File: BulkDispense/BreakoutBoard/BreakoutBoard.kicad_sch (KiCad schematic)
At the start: 35 parts, among them J1 BS1, J10 OS3, J11 OS4, J12 FS1, J13 FS3, J14 PCV, J15 FS2, J16 FS4, J17 WL1, J18 WL2, J19 Analog Inputs, J2 BS2, J20 R0~R3, J21 R4~R7, J22 R8~R9, J23 Digital IN + R0~R4, J24 WB1, J25 WB2, J26 Digital Outputs, J27 R4~R9, J28 WV1, J29 WV2, J3 OS1, J30 Flow Sensors, J4 OS2, J5 PS, J6 MV1&2, J7 MV3&4, J8 BS3, J9 BS4

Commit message: Design Overhaul
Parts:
- removed J1: BS1, PartsLibrary:3720362A3003PL, symbol Connector:Conn_01x03_Socket
- removed J10: OS3, PartsLibrary:3720362A3003PL, symbol Connector:Conn_01x03_Socket
- removed J11: OS4, PartsLibrary:3720362A3003PL, symbol Connector:Conn_01x03_Socket
- removed J19: Analog Inputs, PartsLibrary:CONN_37212-62M3-003PL_3MM, symbol Connector:Conn_01x12_Socket
- removed J2: BS2, PartsLibrary:3720362A3003PL, symbol Connector:Conn_01x03_Socket
- removed J21: R4~R7, PartsLibrary:CONN_37204-62A3-004PL_3MM, symbol Connector:Conn_01x04_Socket
- removed J22: R8~R9, PartsLibrary:CONN_37204-62A3-004PL_3MM, symbol Connector:Conn_01x04_Socket
- removed J26: Digital Outputs, PartsLibrary:CONN_37212-62M3-003PL_3MM, symbol Connector:Conn_01x12_Socket
- removed J28: WV1, PartsLibrary:3720362A3003PL, symbol Connector:Conn_01x03_Socket
- removed J29: WV2, PartsLibrary:3720362A3003PL, symbol Connector:Conn_01x03_Socket
- removed J3: OS1, PartsLibrary:3720362A3003PL, symbol Connector:Conn_01x03_Socket
- removed J4: OS2, PartsLibrary:3720362A3003PL, symbol Connector:Conn_01x03_Socket
- removed J8: BS3, PartsLibrary:3720362A3003PL, symbol Connector:Conn_01x03_Socket
- removed J9: BS4, PartsLibrary:3720362A3003PL, symbol Connector:Conn_01x03_Socket
- removed MAXI1: ~, symbol SymbolLibrary:Controllino_MAXI
- added H5: MountingHole, MountingHole:MountingHole_3.2mm_M3, symbol Mechanical:MountingHole
- added J13: DigitalOUT 0~3, PartsLibrary:CONN_37204-62A3-004PL_3MM, symbol Connector:Conn_01x04_Socket
- added J14: DigitalOUT 4~7, PartsLibrary:CONN_37204-62A3-004PL_3MM, symbol Connector:Conn_01x04_Socket
- added J18: WB-MV1&2, PartsLibrary:CONN_37204-62A3-004PL_3MM, symbol Connector:Conn_01x04_Socket
- added J19: WB-MV3&4, PartsLibrary:CONN_37204-62A3-004PL_3MM, symbol Connector:Conn_01x04_Socket
- added J20: FS1, PartsLibrary:CONN_37204-62A3-004PL_3MM, symbol Connector:Conn_01x04_Socket
- added J22: WB-MV5&6, PartsLibrary:3720362A3003PL, symbol Connector:Conn_01x03_Socket
- H1, H2, H3, H4: footprint MountingHole:MountingHole_2.2mm_M2 -> MountingHole:MountingHole_3.2mm_M3
- J10: renamed from J23; value Digital IN + R0~R4 -> R0~R5
- J17: renamed from J27; value R4~R9 -> AnalogIOs
- J21: renamed from J30; value Flow Sensors -> FS2~FS4
- J4: renamed from J20; value R0~R3 -> RV1~4
- renumbered J5 to J1, J17 to J11, J18 to J12, J24 to J15, J25 to J16, J6 to J2, J7 to J3, J14 to J5, J12 to J6, J13 to J7, J15 to J8, J16 to J9
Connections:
- net DI0 is gone; now on net +24V: J10.1 (Pin_1)
- net DI1 is gone; now on net +24V: J10.2 (Pin_2)
- net DI2 is gone; now on net +24V: J10.3 (Pin_3)
- net DI3 is gone; now on net +24V: J10.4 (Pin_4)
- net R7_OUT is gone; now on net +24V: J17.10 (Pin_10)
- net R9_OUT is gone; now on net GND: J17.12 (Pin_12)
- net +24V: no longer J10.7 (Pin_7), J10.8 (Pin_8), J17.1 (Pin_1), J17.2 (Pin_2), J17.3 (Pin_3), J17.4 (Pin_4), J17.5 (Pin_5), J17.6 (Pin_6)
- net AI12: now also J17.5 (Pin_5)
- net AI13: now also J17.6 (Pin_6)
- net AI4: now also J17.1 (Pin_1)
- net AI5: now also J17.2 (Pin_2)
- net AI6: now also J17.3 (Pin_3)
- net AI7: now also J17.4 (Pin_4)
- net AO0: now also J17.8 (Pin_8); no longer J21.11 (Pin_11)
- net DO0: now also J13.1 (Pin_1)
- net DO1: now also J13.2 (Pin_2)
- net DO2: now also J13.3 (Pin_3)
- net DO3: now also J13.4 (Pin_4)
- net FS1-1: now also J20.1 (Pin_1)
- net FS1-2: now also J20.2 (Pin_2)
- net FS1-3: now also J20.3 (Pin_3)
- net FS1-4: now also J20.4 (Pin_4)
- net FS2-1: now also J21.1 (Pin_1)
- net FS2-2: now also J21.2 (Pin_2)
- net FS2-3: now also J21.3 (Pin_3); no longer J21.1 (Pin_1)
- net FS2-4: now also J21.4 (Pin_4); no longer J21.2 (Pin_2)
- net FS3-1: now also J21.5 (Pin_5); no longer J21.3 (Pin_3)
- net FS3-2: now also J21.6 (Pin_6); no longer J21.4 (Pin_4)
- net FS3-3: now also J21.7 (Pin_7); no longer J21.5 (Pin_5)
- net FS3-4: now also J21.8 (Pin_8); no longer J21.6 (Pin_6)
- net FS4-1: now also J21.9 (Pin_9); no longer J21.7 (Pin_7)
- net FS4-2: now also J21.10 (Pin_10); no longer J21.8 (Pin_8)
- net FS4-3: now also J21.11 (Pin_11); no longer J21.9 (Pin_9)
- net FS4-4: now also J21.12 (Pin_12); no longer J21.10 (Pin_10)
- net GND: now also J18.2 (Pin_2), J18.4 (Pin_4), J19.2 (Pin_2), J19.4 (Pin_4)
- net R0_OUT: now also J10.7 (Pin_7); no longer J10.9 (Pin_9)
- net R1_OUT: now also J10.8 (Pin_8); no longer J10.10 (Pin_10)
- net R2_OUT: now also J10.9 (Pin_9); no longer J10.11 (Pin_11)
- net R3_OUT: now also J10.10 (Pin_10); no longer J10.12 (Pin_12)
- net R4_OUT: now also J10.11 (Pin_11), J22.1 (Pin_1); no longer J17.7 (Pin_7)
- net R5_OUT: now also J10.12 (Pin_12), J22.3 (Pin_3); no longer J17.8 (Pin_8)
- net R6_OUT: no longer names the net of J17.9 (Pin_9)
- net R8_OUT: no longer names the net of J17.11 (Pin_11)
- new net DO4: J14.1 (Pin_1), J18.1 (Pin_1)
- new net DO5: J14.2 (Pin_2), J18.3 (Pin_3)
- new net DO6: J14.3 (Pin_3), J19.1 (Pin_1)
- new net DO7: J14.4 (Pin_4), J19.3 (Pin_3)
- no-connect marks 1 -> 4
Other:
- note added: "WB-MV1"
- note added: "WB-MV2"
- note added: "WB-MV3"
- note added: "WB-MV4"
- note removed: "Relays"
- moved on the sheet: J1, J10, J15, J16, J17, J2, J21, J3, J4, J5, J6, J7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

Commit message: Add latest design
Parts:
- added J24: LDS, PartsLibrary:CONN_37204-62A3-004PL_3MM, symbol Connector:Conn_01x04_Socket
- J11, J12, J15, J16, J22: footprint PartsLibrary:3720362A3003PL -> PartsLibrary:CONN_37203-62A3-003PL_3MM
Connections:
- net +24V: now also J17.11 (Pin_11); no longer J17.10 (Pin_10)
- net AO0: now also J17.7 (Pin_7); no longer J17.8 (Pin_8)
- net LDS-GND: now reaches J17.9 (Pin_9)
- net LDS-GND: now also J24.2 (Pin_2)
- new net LDS: J17.10 (Pin_10), J24.3 (Pin_3)
- new net LDS-5V: J17.8 (Pin_8), J24.1 (Pin_1)
- no-connect marks 4 -> 2
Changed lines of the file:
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@@
 	(rectangle
 		(start 21.59 57.15)
-		(end 106.68 157.48)
+		(end 106.68 180.34)
 		(stroke
 			(width 0)
@@
 	)
 	(rectangle
+		(start 24.13 154.94)
+		(end 63.5 176.53)
+		(stroke
+			(width 0)
+			(type dash)
+		)
+		(fill
+			(type none)
+		)
+	)
+	(rectangle
 		(start 220.98 38.1)
 		(end 256.54 78.74)
@@
 		)
 	)
+	(text_box "Leak Detection"
+		(exclude_from_sim no)
+		(at 44.45 167.64 0)
+		(size 16.51 7.62)
+		(margins 0.9525 0.9525 0.9525 0.9525)
+		(stroke
+			(width -0.0001)
+			(type solid)
+		)
+		(fill
+			(type none)
+		)
+		(effects
+			(font
+				(size 1.27 1.27)
+			)
+			(justify right bottom)
+		)
+	)
 	(text_box "Waste Bottle\n2/2 Media Valves"
 		(exclude_from_sim no)
@@
 	)
 	(no_connect
-		(at 190.5 125.73)
-	)
-	(no_connect
-		(at 190.5 115.57)
-	)
-	(no_connect
-		(at 190.5 120.65)
+		(at 36.83 168.91)
 	)
 	(no_connect
@@
 	(wire
 		(pts
+			(xy 36.83 161.29) (xy 38.1 161.29)
+		)
+		(stroke
+			(width 0)
+			(type default)
+		)
+	)
+	(wire
+		(pts
 			(xy 160.02 64.77) (xy 162.56 64.77)
 		)
@@
 	(wire
 		(pts
+			(xy 36.83 163.83) (xy 38.1 163.83)
+		)
+		(stroke
+			(width 0)
+			(type default)
+		)
+	)
+	(wire
+		(pts
 			(xy 219.71 125.73) (xy 220.98 125.73)
 		)
@@
 	(wire
 		(pts
+			(xy 36.83 166.37) (xy 38.1 166.37)
+		)
+		(stroke
+			(width 0)
+			(type default)
+		)
+	)
+	(wire
+		(pts
 			(xy 142.24 118.11) (xy 143.51 118.11)
 		)
@@
 	(wire
 		(pts
+			(xy 36.83 168.91) (xy 38.1 168.91)
+		)
+		(stroke
+			(width 0)
+			(type default)
+		)
+	)
+	(wire
+		(pts
 			(xy 190.5 107.95) (xy 191.77 107.95)
 		)
@@
 		)
 	)
-	(hierarchical_label "GND"
+	(hierarchical_label "R4_IN"
 		(shape input)
-		(at 190.5 128.27 180)
+		(at 142.24 110.49 180)
 		(effects
 			(font
@@
 		)
 	)
-	(hierarchical_label "R4_IN"
+	(hierarchical_label "LDS-GND"
 		(shape input)
-		(at 142.24 110.49 180)
+		(at 190.5 120.65 180)
 		(effects
 			(font
@@
 		)
 	)
+	(hierarchical_label "LDS"
+		(shape input)
+		(at 36.83 166.37 180)
+		(effects
+			(font
+				(size 1.27 1.27)
+			)
+			(justify right)
+		)
+	)
 	(hierarchical_label "GND"
 		(shape input)
@@
 		)
 	)
+	(hierarchical_label "AO0"
+		(shape input)
+		(at 190.5 115.57 180)
+		(effects
+			(font
+				(size 1.27 1.27)
+			)
+			(justify right)
+		)
+	)
 	(hierarchical_label "R0_IN"
 		(shape input)
@@
 		)
 	)
+	(hierarchical_label "LDS"
+		(shape input)
+		(at 190.5 123.19 180)
+		(effects
+			(font
+				(size 1.27 1.27)
+			)
+			(justify right)
+		)
+	)
 	(hierarchical_label "R2_IN"
 		(shape input)
@@
 		)
 	)
-	(hierarchical_label "AO0"
+	(hierarchical_label "GND"
 		(shape input)
-		(at 190.5 118.11 180)
+		(at 190.5 128.27 180)
 		(effects
 			(font
@@
 		)
 	)
-	(hierarchical_label "24V"
+	(hierarchical_label "DO3"
 		(shape input)
-		(at 190.5 123.19 180)
+		(at 162.56 107.95 180)
 		(effects
 			(font
@@
 		)
 	)
-	(hierarchical_label "DO3"
+	(hierarchical_label "FS3-1"
 		(shape input)
-		(at 162.56 107.95 180)
+		(at 73.66 113.03 180)
 		(effects
 			(font
@@
 		)
 	)
-	(hierarchical_label "FS3-1"
+	(hierarchical_label "24V"
 		(shape input)
-		(at 73.66 113.03 180)
+		(at 190.5 125.73 180)
 		(effects
 			(font
@@
 		)
 	)
+	(hierarchical_label "LDS-5V"
+		(shape input)
+		(at 190.5 118.11 180)
+		(effects
+			(font
+				(size 1.27 1.27)
+			)
+			(justify right)
+		)
+	)
 	(hierarchical_label "R3_IN"
 		(shape input)
@@
 		)
 	)
+	(hierarchical_label "LDS-GND"
+		(shape input)
+		(at 36.83 163.83 180)
+		(effects
+			(font
+				(size 1.27 1.27)
+			)
+			(justify right)
+		)
+	)
 	(hierarchical_label "DO5"
 		(shape input)
@@
 		)
 	)
+	(hierarchical_label "LDS-5V"
+		(shape input)
+		(at 36.83 161.29 180)
+		(effects
+			(font
+				(size 1.27 1.27)
+			)
+			(justify right)
+		)
+	)
 	(symbol
 		(lib_id "Connector:Conn_01x04_Socket")
@@
 	)
 	(symbol
+		(lib_id "Connector:Conn_01x04_Socket")
+		(at 43.18 163.83 0)
+		(unit 1)
+		(exclude_from_sim no)
+		(in_bom yes)
+		(on_board yes)
+		(dnp no)
+		(property "Reference" "J24"
+			(at 44.45 161.29 0)
+			(effects
+				(font
+					(size 1.27 1.27)
+				)
+				(justify left)
+			)
+		)
+		(property "Value" "LDS"
+			(at 44.45 163.83 0)
+			(effects
+				(font
+					(size 1.27 1.27)
+				)
+				(justify left)
+			)
+		)
+		(property "Footprint" "PartsLibrary:CONN_37204-62A3-004PL_3MM"
+			(at 43.18 163.83 0)
+			(effects
+				(font
+					(size 1.27 1.27)
+				)
+				(hide yes)
+			)
+		)
+		(property "Datasheet" "https://www.digikey.com/en/products/detail/3m/37204-62A3-004PL/1642670?gad_source=1&gad_campaignid=120565755&gbraid=0AAAAADrbLlgST8MM7teC1_XRzEHPwC9TK&gclid=CjwKCAjwgb_CBhBMEiwA0p3oONiHu6nwJTm_ZwqulepAmgPW2KMjOTu2fKjs93rH9sOuJqpPoBx-0hoCrs0QAvD_BwE&gclsrc=aw.ds"
+			(at 43.18 163.83 0)
+			(effects
+				(font
+					(size 1.27 1.27)
+				)
+				(hide yes)
+			)
+		)
+		(property "Description" "CONN RCPT 4POS 0.079 GOLD PCB"
+			(at 43.18 163.83 0)
+			(effects
+				(font
+					(size 1.27 1.27)
+				)
+				(hide yes)
+			)
+		)
+		(property "MPN" "37204-62A3-004PL"
+			(at 43.18 163.83 0)
+			(effects
+				(font
+					(size 1.27 1.27)
+				)
+				(hide yes)
+			)
+		)
+		(property "Manufacturer" "3M"
+			(at 43.18 163.83 0)
+			(effects
+				(font
+					(size 1.27 1.27)
+				)
+				(hide yes)
+			)
+		)
+		(pin "1"
+		)
+		(pin "3"
+		)
+		(pin "2"
+		)
+		(pin "4"
+		)
+		(instances
+			(project "BreakoutBoard"
+				(path "/a97e9ae7-7c53-4daf-85b8-910ef7d9e636"
+					(reference "J24")
+					(unit 1)
+				)
+			)
+		)
+	)
+	(symbol
 		(lib_id "power:+24V")
 		(at 53.34 35.56 0)
@@
 			)
 		)
-		(property "Footprint" "PartsLibrary:3720362A3003PL"
+		(property "Footprint" "PartsLibrary:CONN_37203-62A3-003PL_3MM"
 			(at 167.64 50.8 0)
 			(effects
@@
 			)
 		)
-		(property "Footprint" "PartsLibrary:3720362A3003PL"
+		(property "Footprint" "PartsLibrary:CONN_37203-62A3-003PL_3MM"
 			(at 137.16 49.53 0)
 			(effects
@@
 			)
 		)
-		(property "Footprint" "PartsLibrary:3720362A3003PL"
+		(property "Footprint" "PartsLibrary:CONN_37203-62A3-003PL_3MM"
 			(at 167.64 67.31 0)
 			(effects
@@
 			)
 		)
-		(property "Footprint" "PartsLibrary:3720362A3003PL"
+		(property "Footprint" "PartsLibrary:CONN_37203-62A3-003PL_3MM"
 			(at 137.16 66.04 0)
 			(effects
@@
 			)
 		)
-		(property "Footprint" "PartsLibrary:3720362A3003PL"
+		(property "Footprint" "PartsLibrary:CONN_37203-62A3-003PL_3MM"
 			(at 240.03 58.42 0)
 			(effects

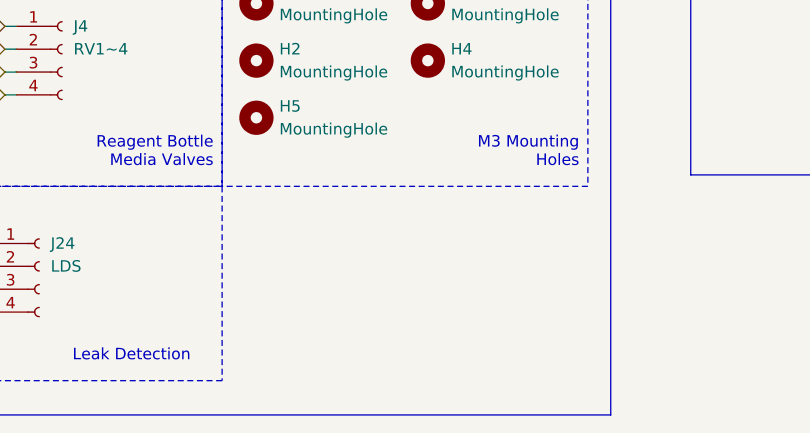
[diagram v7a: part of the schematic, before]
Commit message: Edit BOM
Format BOM to PCBWay's Request
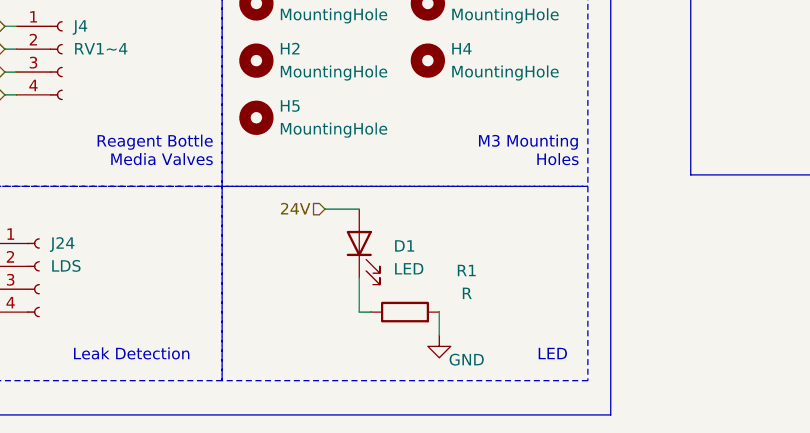
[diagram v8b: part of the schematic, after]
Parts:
- added D1: LED, LED_SMD:LED_1206_3216Metric, symbol Device:LED
- added R1: R, Resistor_SMD:R_0805_2012Metric, symbol Device:R
- J1, J13, J14, J18, J19, J2, J20, J3, J4, J5, J6, J7, J8, J9: MPN (none) -> 37204-62A3-004PL; Manufacturer (none) -> 3M
- J10, J17, J21: MPN (none) -> 37212-62M3-003PL; Manufacturer (none) -> 3M
- J11, J12, J15, J16, J22: MPN (none) -> 37203-62A3-003PL; Manufacturer (none) -> 3M
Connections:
- net +24V: now also D1.2 (A)
- net GND: now also R1.2
- new net: D1.1 (K), R1.1
